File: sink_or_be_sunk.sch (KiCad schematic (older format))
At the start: 1 part

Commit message: first iteration of main pcb
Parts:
- added C1: 100uF, Capacitor_SMD:C_0805_2012Metric_Pad1.15x1.40mm_HandSolder, symbol Device:C
- added D1: D_Zener, Diode_SMD:D_0805_2012Metric_Pad1.15x1.40mm_HandSolder, symbol Device:D_Zener
- added J1: AudioJack2_Ground, Connector_BarrelJack:BarrelJack_CUI_PJ-102AH_Horizontal, symbol Connector:AudioJack2_Ground
- added J2: Conn_01x05_Male, Connector_PinHeader_2.54mm:PinHeader_1x05_P2.54mm_Horizontal, symbol Connector:Conn_01x05_Male
- added J3: Conn_01x08_Male, Connector_PinSocket_2.54mm:PinSocket_1x08_P2.54mm_Vertical, symbol Connector:Conn_01x08_Male
- added J4: Conn_01x08_Male, Connector_PinHeader_2.54mm:PinHeader_1x08_P2.54mm_Vertical, symbol Connector:Conn_01x08_Male
- added LS1: Speaker, symbol Device:Speaker
- added M1: Motor_DC, Connector_PinHeader_2.54mm:PinHeader_1x02_P2.54mm_Vertical, symbol Motor:Motor_DC
- added Q1: IRLML5203, Package_TO_SOT_SMD:SOT-23, symbol Transistor_FET:IRLML5203
- added R1, R2, R3, R4: 1k, Resistor_SMD:R_0805_2012Metric_Pad1.15x1.40mm_HandSolder, symbol Device:R
- added RV1: R_POT, symbol Device:R_POT
- added U2: MCP601-xP, Package_DIP:DIP-8_W7.62mm, symbol Amplifier_Operational:MCP601-xP
- added U3: SN74HC151N, PCB_ESP32:SN74HC151N-PDIP, symbol grid:SN74HC151N
- added U6: LDL1117-SMD, Package_TO_SOT_SMD:SOT-223, symbol grid:LDL1117-SMD
- gave numbers to parts that had none: 1
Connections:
- net BOAT_INPUT: now also U3.5 (Y)
- net DAC_OUT: now also U2.3 (+)
- net GND: now also U1.1 (GND), U1.15 (GND), U1.38 (GND), U1.39 (GND), C1.2, J1.G, J2.1 (Pin_1), LS1.2, Q1.2 (S), RV1.3, U2.4 (V-), U3.7 (~G), U3.8 (GND), U6.1 (GND)
- net KEYPAD_IN0: now also R1.2
- net KEYPAD_IN1: now also R2.2
- net KEYPAD_IN2: now also R3.2
- net KEYPAD_IN3: now also R4.2
- net KEYPAD_OUT0: now also J3.5 (Pin_5)
- net KEYPAD_OUT1: now also J3.6 (Pin_6)
- net KEYPAD_OUT2: now also J3.7 (Pin_7)
- net KEYPAD_OUT3: now also J3.8 (Pin_8)
- net LCD_CS: now also J2.5 (Pin_5)
- net LCD_MOSI: now also J2.4 (Pin_4)
- net LCD_SCLK: now also J2.3 (Pin_3)
- net MOTOR: now also Q1.1 (G)
- net MUX_ROW_SEL0: now also U3.11 (A)
- net MUX_ROW_SEL1: now also U3.10 (B)
- net MUX_ROW_SEL2: now also U3.9 (C)
- net SHD_SD2: now reaches U1.17 (SHD/SD2)
- net SWP_SD3: now reaches U1.18 (SWP/SD3)
- net SCS_CMD: now reaches U1.19 (SCS/CMD)
- net +3V3: now reaches U1.2 (VDD)
- net +3V3: now also U6.4 (VOUT)
- net SCK_CLK: now reaches U1.20 (SCK/CLK)
- net SDO_SD0: now reaches U1.21 (SDO/SD0)
- net SDI_SD1: now reaches U1.22 (SDI/SD1)
- net X: now reaches U1.25 (IO0)
- net X: now also U6.2 (VOUT)
- net EN: now reaches U1.3 (EN)
- net SENSOR_VP: now reaches U1.4 (SENSOR_VP)
- net SENSOR_VN: now reaches U1.5 (SENSOR_VN)
- new net: RV1.1, U2.2 (-), U2.6
- new net: LS1.1, RV1.2
- new net: J3.1 (Pin_1), R1.1
- new net: J3.2 (Pin_2), R2.1
- new net: J3.3 (Pin_3), R3.1
- new net: J3.4 (Pin_4), R4.1
- new net: D1.2 (A), Q1.3 (D)
- new net: D1.1 (K), M1.2 (-)
- new net: J1.T, U6.3 (VIN)
- new net +5V: J2.2 (Pin_2), M1.1 (+)
- new net MUX_ROW0: J4.1 (Pin_1), U3.4 (D0)
- new net MUX_ROW1: J4.2 (Pin_2), U3.3 (D1)
- new net MUX_ROW2: J4.3 (Pin_3), U3.2 (D2)
- new net MUX_ROW3: J4.4 (Pin_4), U3.1 (D3)
- new net MUX_ROW4: J4.5 (Pin_5), U3.15 (D4)
- new net MUX_ROW5: J4.6 (Pin_6), U3.14 (D5)
- new net MUX_ROW6: J4.7 (Pin_7), U3.13 (D6)
- new net MUX_ROW7: J4.8 (Pin_8), U3.12 (D7)
- new net VDD: C1.1, U2.7 (V+), U3.16 (VCC)
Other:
- note added: "In reference to microcontroller:\nrows are "outputs"\ncols are "inputs""
- note added: "LCD:\nPIN | Signal\n3 | VSS\n4 | VDD\n5 | SCLK\n6 | SID\n8 | CS"
- note added: "NOTE: we have the MCP608 \non the parts list but this looks \nlike the same package"
- note added: "Re-using footprint\n for CUI_PJ-102"
- note added: "Supply Decoupling"
- note added: "TODO: \n\n- Connect the sheets \n(mitch, you might have to help me with this)\n\n- Double check schematic for audio jack\n\n- footprints for speaker/pot\n"
- note added: "This has the same foot print as SOT223"
- note added: "To Do:\nAre the signals \nabove and below \nbeing used anywhere?"
- note removed: "TODO: Connect up sheets and add additional components (motor drivers, speakers, etc...)"
- moved on the sheet: U1

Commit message: cleaned up files
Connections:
- net X: now also J1.S
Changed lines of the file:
@@
 Wire Notes Line
 	4000 5000 4000 7750
+Wire Wire Line
+	1250 7000 1400 7000
+Text Label 1400 7000 1    50   ~ 0
+X
 $EndSCHEMATC

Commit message: check speaker pot footprint
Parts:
- LS1: footprint (none) -> Connector_PinHeader_2.54mm:PinHeader_1x02_P2.54mm_Horizontal
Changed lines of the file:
@@
 F 0 "LS1" H 10850 1050 50  0000 L CNN
 F 1 "Speaker" H 10800 950 50  0000 L CNN
-F 2 "" H 10900 1100 50  0001 C CNN
+F 2 "Connector_PinHeader_2.54mm:PinHeader_1x02_P2.54mm_Horizontal" H 10900 1100 50  0001 C CNN
 F 3 "~" H 10890 1250 50  0001 C CNN
 	1    10900 1300

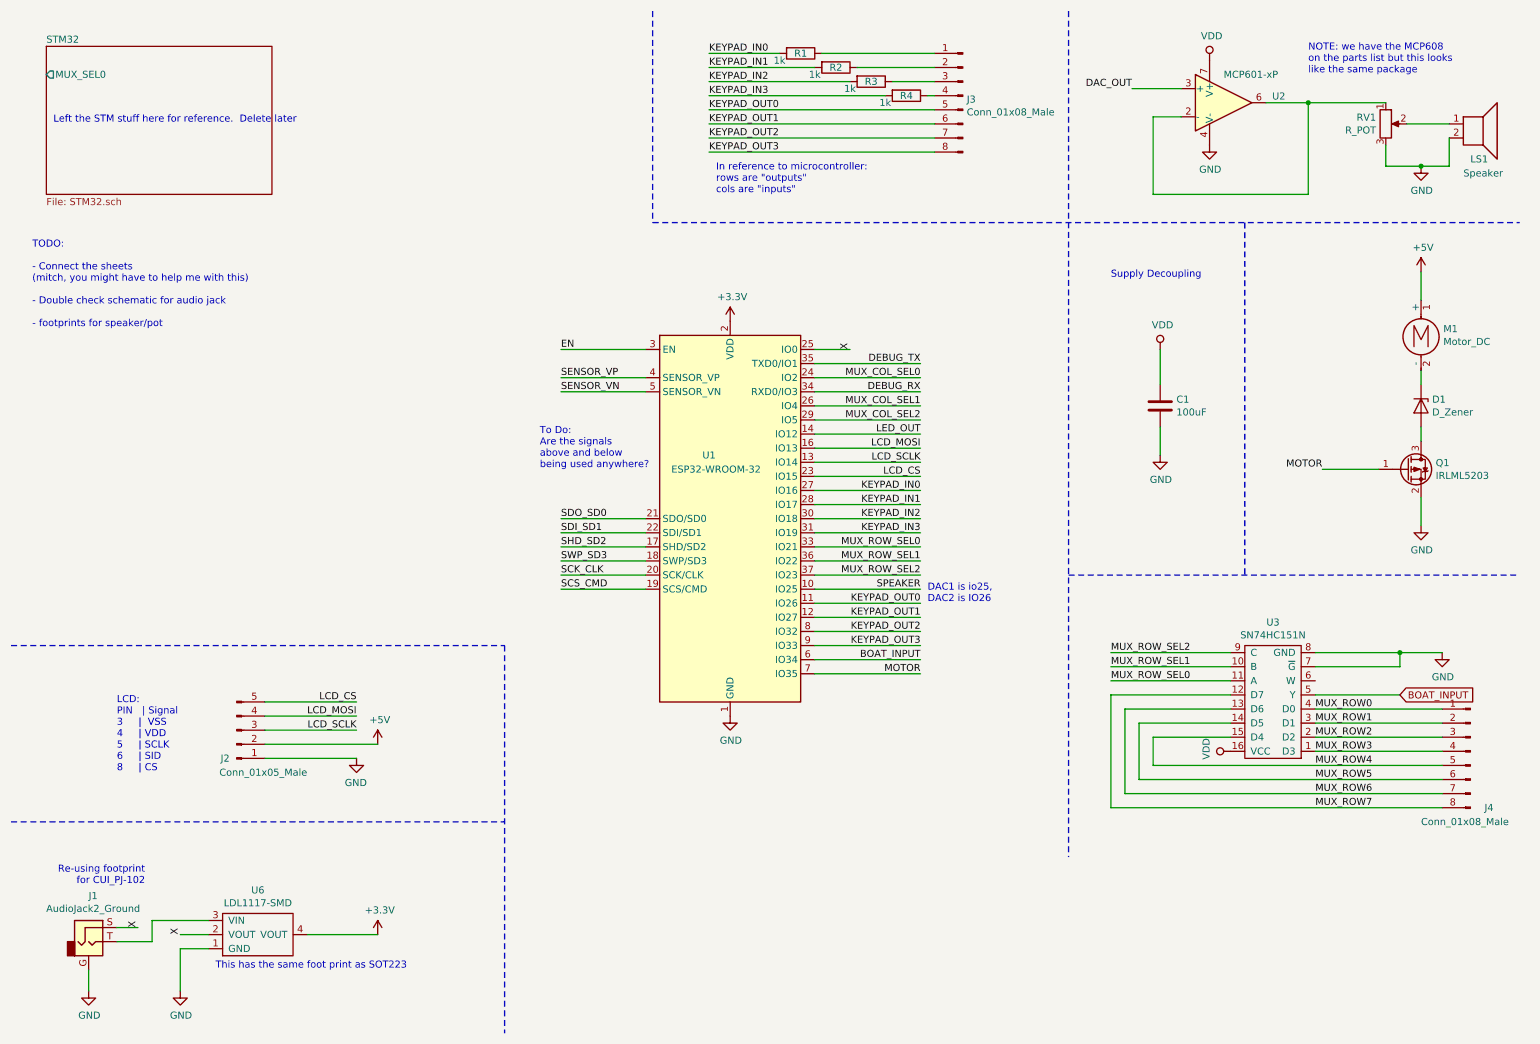
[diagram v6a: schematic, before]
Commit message: added some notes/todos on schematic
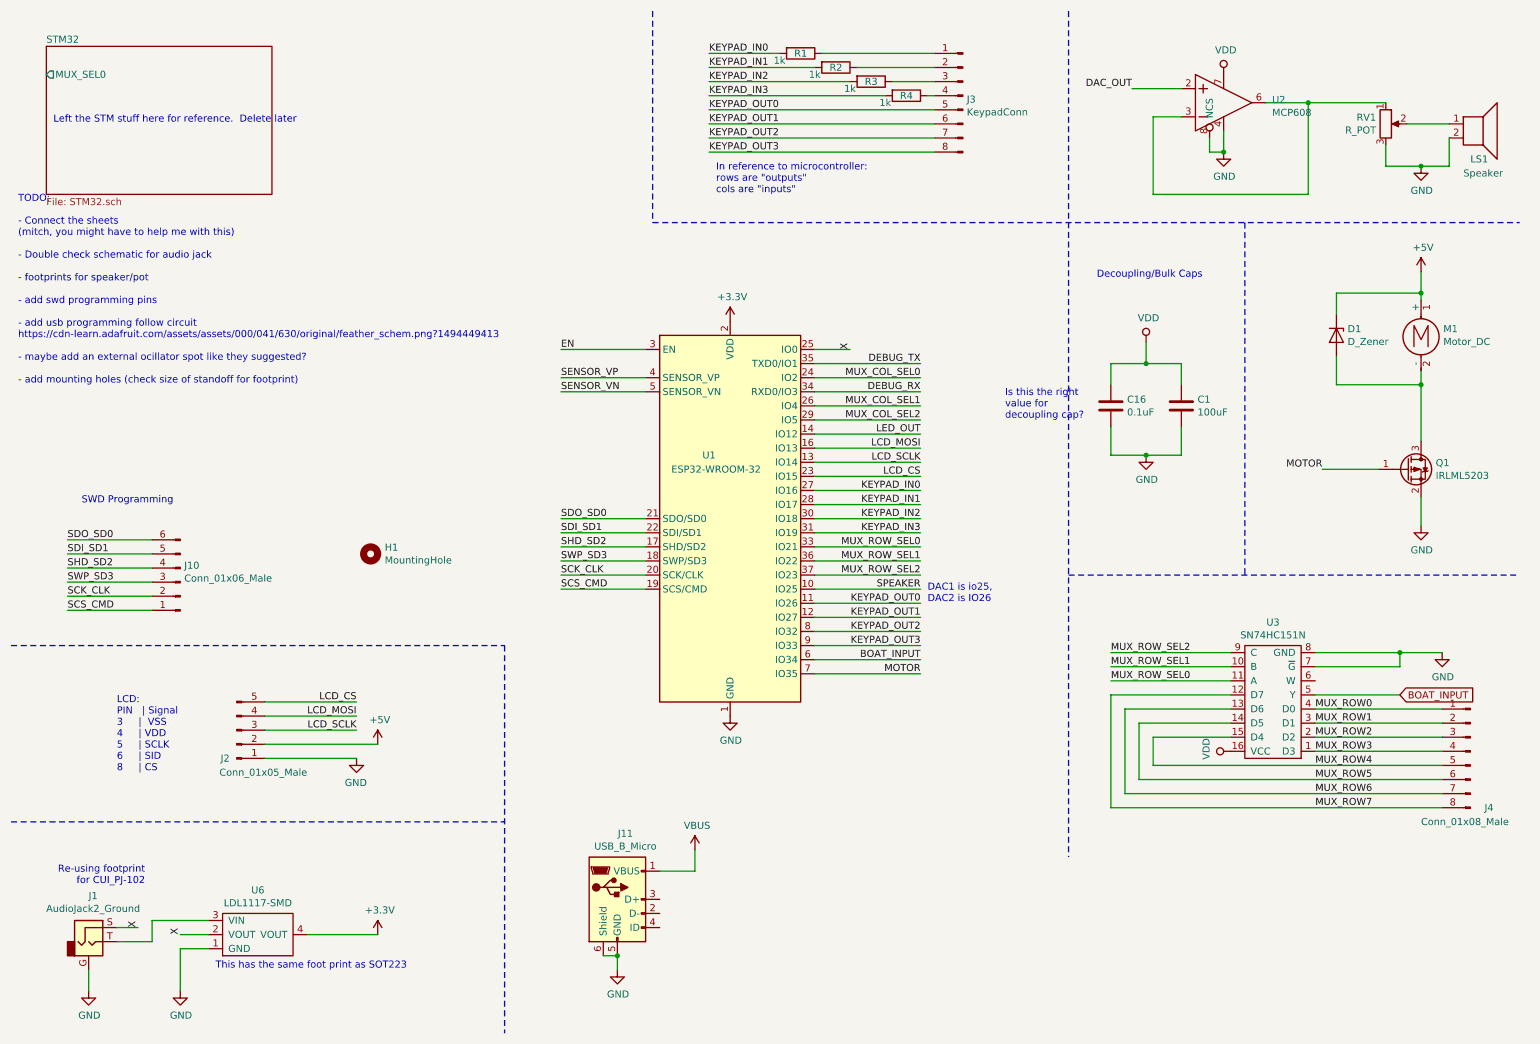
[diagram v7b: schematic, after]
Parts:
- removed U2: MCP601-xP, Package_DIP:DIP-8_W7.62mm, symbol Amplifier_Operational:MCP601-xP
- added C16: 0.1uF, Capacitor_SMD:C_0805_2012Metric_Pad1.15x1.40mm_HandSolder, symbol Device:C
- added H1: MountingHole, symbol Mechanical:MountingHole
- added J10: Conn_01x06_Male, symbol Connector:Conn_01x06_Male
- added J11: USB_B_Micro, symbol Connector:USB_B_Micro
- added U2: MCP608, Package_DIP:DIP-8_W7.62mm, symbol grid:MCP608
- J3: value Conn_01x08_Male -> KeypadConn
- RV1: footprint (none) -> Connector_PinHeader_2.54mm:PinHeader_1x03_P2.54mm_Horizontal
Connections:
- net +5V: now also D1.1 (K)
- net DAC_OUT: now also U2.2
- net GND: now also C16.2, J11.5 (GND), J11.6 (Shield), U2.4, U2.8 (NCS)
- net SCK_CLK: now also J10.2 (Pin_2)
- net SCS_CMD: now also J10.1 (Pin_1)
- net SDI_SD1: now also J10.5 (Pin_5)
- net SDO_SD0: now also J10.6 (Pin_6)
- net SHD_SD2: now also J10.4 (Pin_4)
- net SWP_SD3: now also J10.3 (Pin_3)
- net VDD: now also C16.1, U2.7
- net at RV1.1: now also U2.3, U2.6
- net at D1.2 (A), Q1.3 (D): now also M1.2 (-)
- new net VBUS: J11.1 (VBUS)
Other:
- note added: "Decoupling/Bulk Caps"
- note added: "Is this the right \nvalue for \ndecoupling cap?"
- note added: "SWD Programming"
- note added: "TODO: \n\n- Connect the sheets \n(mitch, you might have to help me with this)\n\n- Double check schematic for audio jack\n\n- footprints for speaker/pot\n\n- add swd programming pins\n\n- add usb programming follow circuit \nhttps://cdn-learn.adafruit.com/assets/assets/000/041/630/original/feather_schem.png?1494449413\n\n- maybe add an external ocillator spot like they suggested?\n\n- add mountin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"
- note removed: "NOTE: we have the MCP608 \non the parts list but this looks \nlike the same package"
- note removed: "Supply Decoupling"
- note removed: "TODO: \n\n- Connect the sheets \n(mitch, you might have to help me with this)\n\n- Double check schematic for audio jack\n\n- footprints for speaker/pot\n"
- note removed: "To Do:\nAre the signals \nabove and below \nbeing used anywhere?"
- moved on the sheet: C1, D1

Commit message: updated todo
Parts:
- added C17: C, Capacitor_SMD:C_0805_2012Metric_Pad1.15x1.40mm_HandSolder, symbol Device:C
- added H2, H3, H4: MountingHole, MountingHole:MountingHole_6.4mm_M6, symbol Mechanical:MountingHole
- added Q2, Q3: MMBT5550L, Package_TO_SOT_SMD:SOT-23, symbol Transistor_BJT:MMBT5550L
- added R16, R17: 10k, Resistor_SMD:R_0805_2012Metric_Pad1.15x1.40mm_HandSolder, symbol Device:R
- added U7: CP2104, Package_DFN_QFN:QFN-24-1EP_4x4mm_P0.5mm_EP2.6x2.6mm, symbol Interface_USB:CP2104
- H1: footprint (none) -> MountingHole:MountingHole_6.4mm_M6
- J10: footprint (none) -> Connector_PinHeader_2.54mm:PinHeader_1x06_P2.54mm_Vertical
- J11: footprint (none) -> digikey-footprints:USB_Micro_B_Female_Vert_1051330001; symbol Connector:USB_B_Micro -> sink_or_be_sunk-rescue:USB_B_Micro-Connector
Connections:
- net +3V3: now also C17.1, U7.5 (VIO), U7.6 (VDD), U7.7 (REGIN)
- net GND: now also C17.2, U7.2 (GND)
- net VBUS: now also U7.8 (VBUS)
- net X: now also J11.4 (ID), U7.10 (VIO/NC); no longer U1.25 (IO0)
- net D+: now reaches J11.2 (D-)
- net D+: now also J11.3 (D+), U7.3 (D+), U7.4 (D-)
- net EN renamed RESET
- net RESET: now also Q3.3 (C)
- new net: Q2.1 (B), R16.1
- new net: Q3.1 (B), R17.1
- new net DTR: Q2.2 (E), R17.2, U7.23 (DTR)
- new net GPIO0: Q2.3 (C), U1.25 (IO0)
- new net RTS: Q3.2 (E), R16.2, U7.19 (RTS)
- new net RXD0: U7.20 (RXD)
- new net TXD0: U7.21 (TXD)
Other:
- note added: "Left the STM stuff here for reference. \nDelete later"
- note added: "Still a little unclear on wiring the audio jack\n- I know we really only need to use two pins, unsure of which two"
- note added: "TODO: \n\n- Connect the sheets \n(mitch, you might have to help me with this)\n\n- Double check schematic for audio jack\n\n- footprints for speaker/pot DONE\n\n- add swd programming pins DONE\n\n- add usb programming follow circuit \nhttps://cdn-learn.adafruit.com/assets/assets/000/041/630/original/feather_schem.png?1494449413\n\n- maybe add an external ocillator spot like they suggested?\n\n- a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"
- note added: "Using 7/16" standoff \n(11.13mm tall, 6.35mm diam)\n** Can be changed later **"
- note removed: "Left the STM stuff here for reference. Delete later"
- note removed: "TODO: \n\n- Connect the sheets \n(mitch, you might have to help me with this)\n\n- Double check schematic for audio jack\n\n- footprints for speaker/pot\n\n- add swd programming pins\n\n- add usb programming follow circuit \nhttps://cdn-learn.adafruit.com/assets/assets/000/041/630/original/feather_schem.png?1494449413\n\n- maybe add an external ocillator spot like they suggested?\n\n- add mountin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"
- moved on the sheet: C1, C16, D1, H1, J1, J10, J11, J2, J3, J4, LS1, M1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
